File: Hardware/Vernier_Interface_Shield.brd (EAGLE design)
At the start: 76.2 x 71.1 mm, 44 parts, among them U1 74HC4052SO, U2 LMV358SOICT

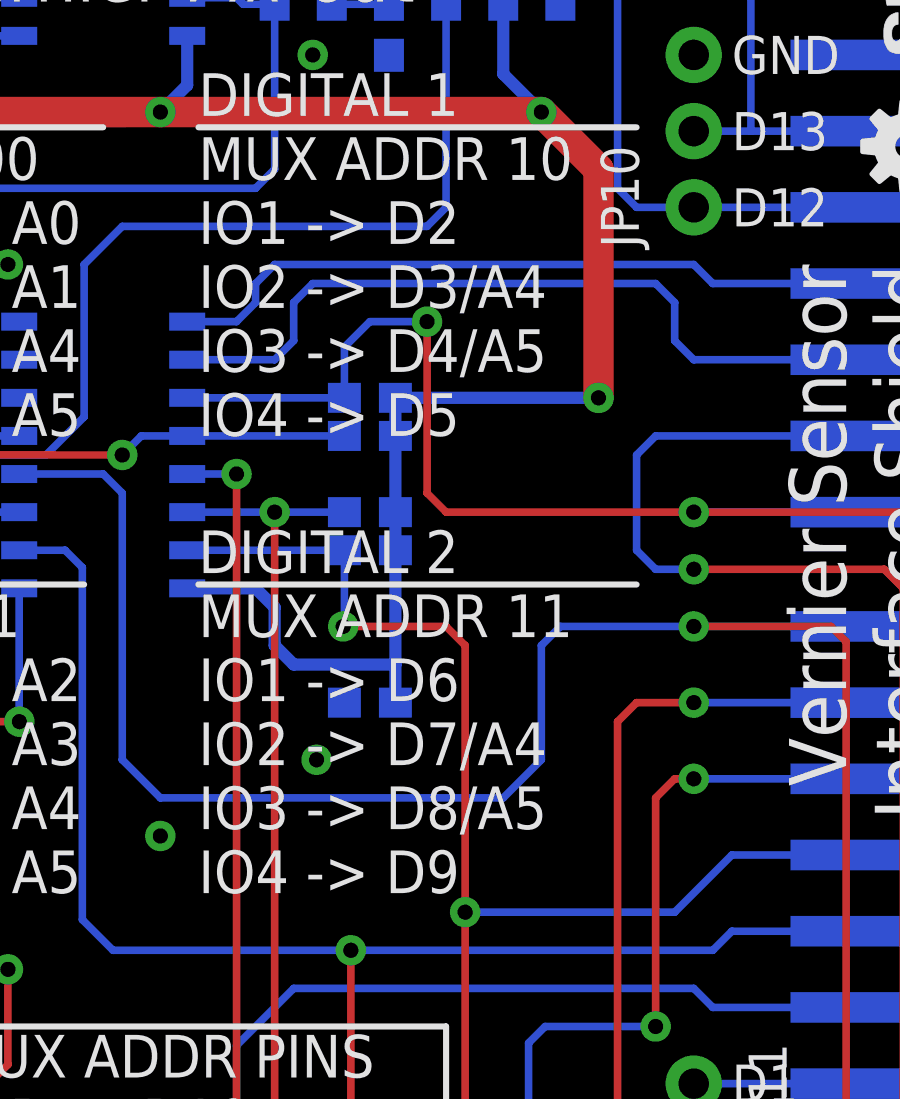
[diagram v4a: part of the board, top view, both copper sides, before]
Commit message: Changed silk to fix bug #4
Changed silk to start at IO0 instead of IO1. This is per Vernier's
request.
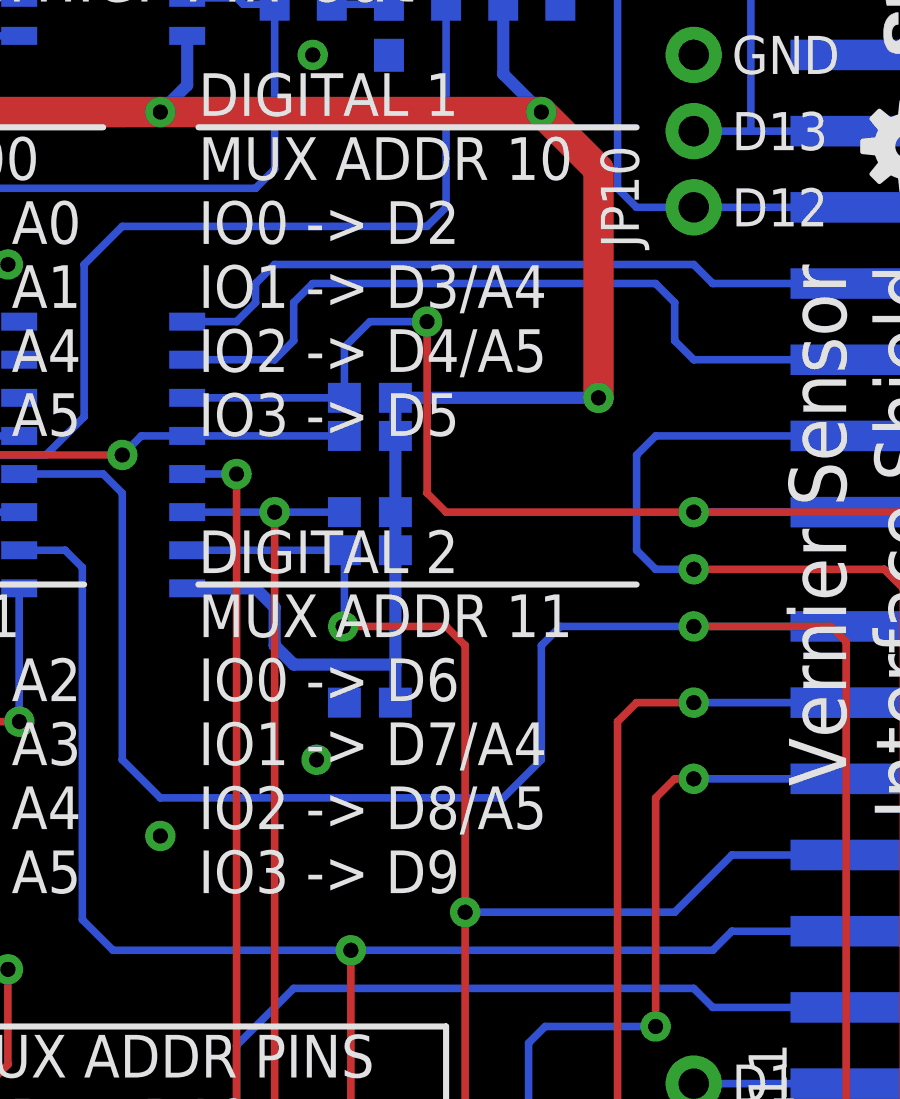
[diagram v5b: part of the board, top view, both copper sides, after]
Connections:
- removed net D1_IO4: JP2.6, JP7.6
- removed net D2_IO4: JP1.2, JP8.6
- new net D1_IO0: JP2.3, JP7.1
- new net D2_IO0: JP2.7, JP8.1
- net D1_IO1: now also JP2.4, JP7.2, U1.2; no longer JP2.3, JP7.1
- net D1_IO2: now also JP2.5, JP7.3, R17.2, U1.15; no longer JP2.4, JP7.2, U1.2
- net D1_IO3: now also JP2.6, JP7.6; no longer JP2.5, JP7.3, R17.2, U1.15
- net D2_IO1: now also JP2.8, JP8.2, U1.4; no longer JP2.7, JP8.1
- net D2_IO2: now also JP1.1, JP8.3, R18.2, U1.11; no longer JP2.8, JP8.2, U1.4
- net D2_IO3: now also JP1.2, JP8.6; no longer JP1.1, JP8.3, R18.2, U1.11
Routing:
- net D2_IO4: track 51.5 -> 0.00 mm, vias 1 -> 0
- net D2_IO0: track 0.00 -> 40.4 mm, vias 0 -> 2
- net D1_IO3: track 70.2 -> 30.6 mm, vias 3 -> 2
- net D1_IO0: track 0.00 -> 37.5 mm
- net D2_IO3: track 86.9 -> 51.5 mm, vias 2 -> 1
- net D2_IO1: track 40.4 -> 74.2 mm
- net D1_IO4: track 30.6 -> 0.00 mm, vias 2 -> 0
- net D1_IO1: track 37.5 -> 55.3 mm, vias 0 -> 1
- net D1_IO2: track 55.3 -> 70.2 mm, vias 1 -> 3
- net D2_IO2: track 74.2 -> 86.9 mm
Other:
- board text added: "DIGITAL 1 MUX ADDR 10 IO0 -> D2 IO1 -> D3/A4 IO2 -> D4/A5 IO3 -> D5"
- board text added: "DIGITAL 2 MUX ADDR 11 IO0 -> D6 IO1 -> D7/A4 IO2 -> D8/A5 IO3 -> D9"
- board text removed: "DIGITAL 1 MUX ADDR 10 IO1 -> D2 IO2 -> D3/A4 IO3 -> D4/A5 IO4 -> D5"
- board text removed: "DIGITAL 2 MUX ADDR 11 IO1 -> D6 IO2 -> D7/A4 IO3 -> D8/A5 IO4 -> D9"
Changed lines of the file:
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@@
 <text x="39.37" y="43.815" size="1.4224" layer="21" font="vector" ratio="15">DIGITAL 1
 MUX ADDR 10
-IO1 -&gt; D2
-IO2 -&gt; D3/A4
-IO3 -&gt; D4/A5
-IO4 -&gt; D5</text>
+IO0 -&gt; D2
+IO1 -&gt; D3/A4
+IO2 -&gt; D4/A5
+IO3 -&gt; D5</text>
 <text x="39.37" y="28.575" size="1.4224" layer="21" font="vector" ratio="15">DIGITAL 2
 MUX ADDR 11
-IO1 -&gt; D6
-IO2 -&gt; D7/A4
-IO3 -&gt; D8/A5
-IO4 -&gt; D9</text>
+IO0 -&gt; D6
+IO1 -&gt; D7/A4
+IO2 -&gt; D8/A5
+IO3 -&gt; D9</text>
 <text x="59.055" y="49.53" size="1.905" layer="21" font="vector" ratio="15" rot="R270">Vernier Sensor
 Interface Shield</text>
@@
 <wire x1="31.75" y1="17.78" x2="33.325" y2="16.205" width="0.254" layer="16"/>
 </signal>
-<signal name="D2_IO4">
+<signal name="D2_IO3">
 <contactref element="JP1" pad="2"/>
 <contactref element="JP8" pad="6"/>
@@
 <wire x1="65.405" y1="15.24" x2="62.865" y2="17.78" width="0.254" layer="1"/>
 </signal>
-<signal name="D2_IO3">
+<signal name="D2_IO2">
 <contactref element="U1" pad="11"/>
 <contactref element="R18" pad="2"/>
@@
 <wire x1="46.99" y1="41.91" x2="46.99" y2="47.625" width="0.254" layer="1"/>
 </signal>
-<signal name="D2_IO2">
+<signal name="D2_IO1">
 <contactref element="U1" pad="4"/>
 <contactref element="JP8" pad="2"/>
@@
 <wire x1="62.103" y1="37.465" x2="55.88" y2="37.465" width="0.254" layer="16"/>
 </signal>
-<signal name="D2_IO1">
+<signal name="D2_IO0">
 <contactref element="JP8" pad="1"/>
 <contactref element="JP2" pad="7"/>
@@
 <wire x1="53.34" y1="19.685" x2="54.61" y2="18.415" width="0.254" layer="1"/>
 </signal>
-<signal name="D1_IO4">
+<signal name="D1_IO3">
 <contactref element="JP7" pad="6"/>
 <via x="54.61" y="24.13" extent="1-16" drill="0.508"/>
@@
 <wire x1="55.245" y1="32.385" x2="54.61" y2="31.75" width="0.254" layer="1"/>
 </signal>
-<signal name="D1_IO3">
+<signal name="D1_IO2">
 <contactref element="U1" pad="15"/>
 <contactref element="R17" pad="2"/>
@@
 <wire x1="55.245" y1="27.94" x2="57.15" y2="29.845" width="0.254" layer="16"/>
 </signal>
-<signal name="D1_IO2">
+<signal name="D1_IO1">
 <contactref element="U1" pad="2"/>
 <contactref element="JP7" pad="2"/>
@@
 <wire x1="56.515" y1="26.67" x2="44.45" y2="26.67" width="0.254" layer="16"/>
 </signal>
-<signal name="D1_IO1">
+<signal name="D1_IO0">
 <contactref element="JP2" pad="3"/>
 <contactref element="JP7" pad="1"/>

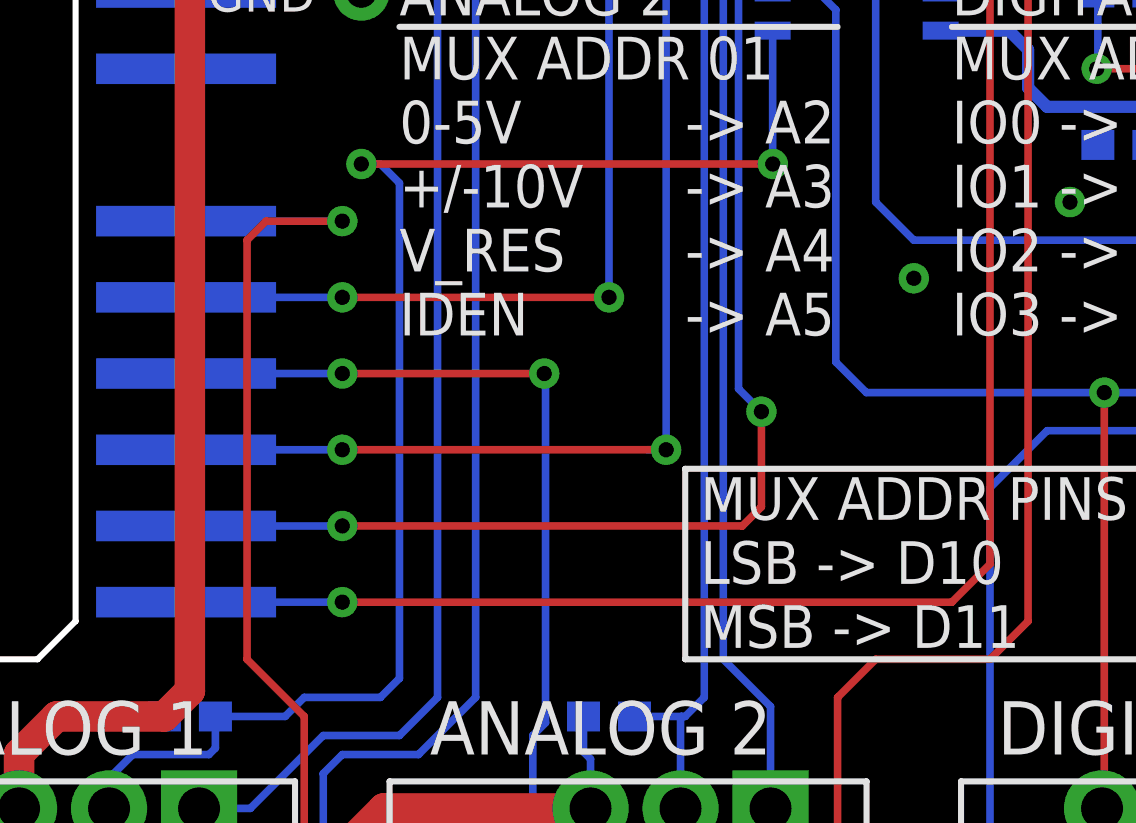
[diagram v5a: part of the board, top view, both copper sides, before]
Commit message: Updated A0-A5 vias to be exposed to allow for probe pins
Swapped out 6 vias on A0 to A5 with M06 for exposed copper vias to allow
for probe points
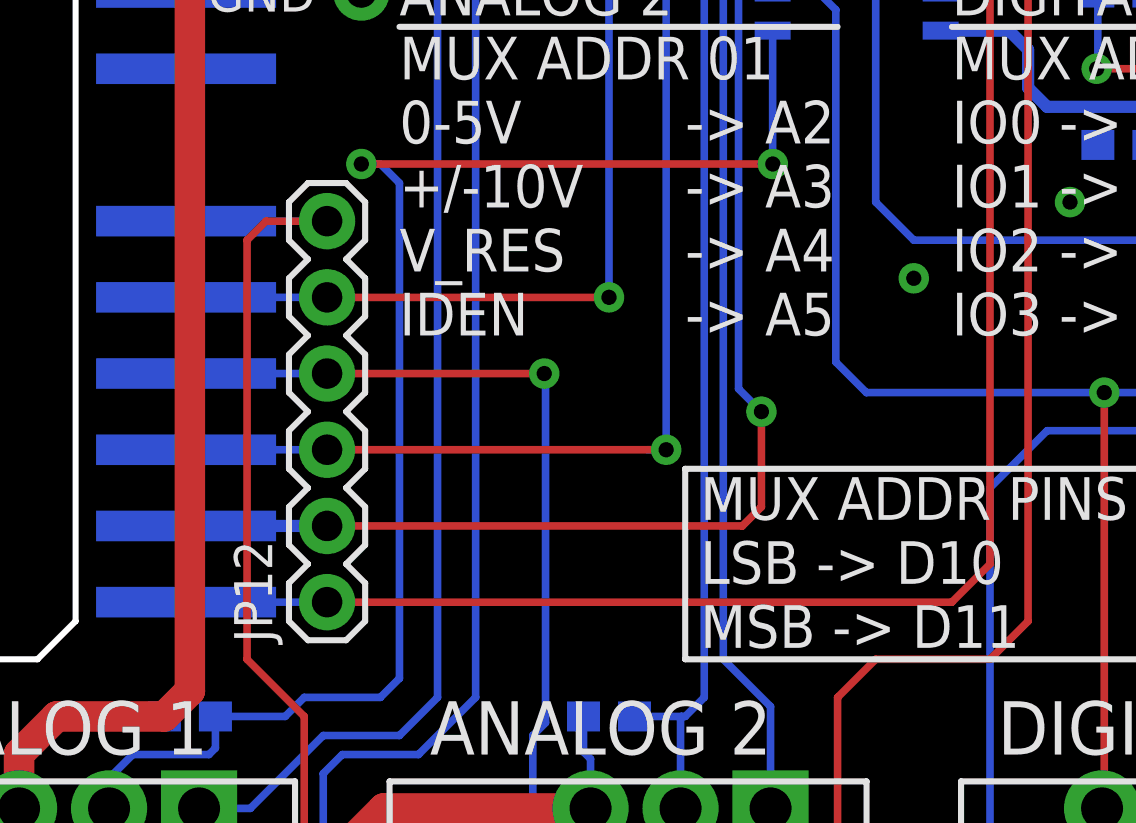
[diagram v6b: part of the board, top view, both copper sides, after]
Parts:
- added JP12: Male, SparkFun-Connectors:1X06
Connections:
- net A1: now also JP12.5
- net A3: now also JP12.3
- net A4: now also JP12.2
- net A5: now also JP12.1
- net AS1_AN2: now also JP12.6
- net AS2_AN2: now also JP12.4
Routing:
- net AS1_AN2: track 46.8 -> 45.8 mm, vias 1 -> 0
- net A5: vias 2 -> 1
- net AS2_AN2: vias 2 -> 1
- net A4: vias 2 -> 1
- net A3: vias 2 -> 1
- net A1: vias 2 -> 1
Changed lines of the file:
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@@
 </class>
 </classes>
-<designrules name="SparkFun *">
+<designrules name="SparkFun-2-layer">
 <description language="en">&lt;b&gt;EAGLE Design Rules&lt;/b&gt;
 &lt;p&gt;
@@
 <param name="mdDrill" value="8mil"/>
 <param name="mdSmdStop" value="0mil"/>
-<param name="msWidth" value="8mil"/>
-<param name="msDrill" value="20mil"/>
+<param name="msWidth" value="7mil"/>
+<param name="msDrill" value="15mil"/>
 <param name="msMicroVia" value="9.99mm"/>
 <param name="msBlindViaRatio" value="0.5"/>
@@
 <element name="S3" library="SparkFun-Electromechanical" package="TACTILE-PTH" value="Reset" x="16.51" y="67.31" rot="R180"/>
 <element name="S4" library="SparkFun-Electromechanical" package="TACTILE-PTH" value="D12" x="45.72" y="67.31" rot="R180"/>
+<element name="JP12" library="SparkFun-Connectors" package="1X06" value="Male" x="18.542" y="19.685" rot="R90"/>
 </elements>
 <signals>
@@
 <contactref element="JP4" pad="2"/>
 <contactref element="U1" pad="3"/>
-<wire x1="13.843" y1="22.225" x2="19.05" y2="22.225" width="0.254" layer="16"/>
-<via x="19.05" y="22.225" extent="1-16" drill="0.508"/>
 <wire x1="33.395" y1="41.275" x2="32.639" y2="41.275" width="0.254" layer="16"/>
 <wire x1="32.639" y1="41.275" x2="32.258" y2="40.894" width="0.254" layer="16"/>
@@
 <via x="33.02" y="26.035" extent="1-16" drill="0.508"/>
 <wire x1="32.258" y1="26.797" x2="33.02" y2="26.035" width="0.254" layer="16"/>
-<wire x1="19.05" y1="22.225" x2="32.385" y2="22.225" width="0.254" layer="1"/>
+<wire x1="18.542" y1="22.225" x2="32.385" y2="22.225" width="0.254" layer="1"/>
 <wire x1="32.385" y1="22.225" x2="33.02" y2="22.86" width="0.254" layer="1"/>
 <wire x1="33.02" y1="22.86" x2="33.02" y2="26.035" width="0.254" layer="1"/>
+<contactref element="JP12" pad="2"/>
+<wire x1="18.542" y1="22.225" x2="13.843" y2="22.225" width="0.4064" layer="16"/>
 </signal>
 <signal name="A5">
@@
 <wire x1="40.64" y1="42.545" x2="40.64" y2="20.955" width="0.254" layer="1"/>
 <wire x1="40.64" y1="20.955" x2="39.37" y2="19.685" width="0.254" layer="1"/>
-<wire x1="39.37" y1="19.685" x2="19.05" y2="19.685" width="0.254" layer="1"/>
-<via x="19.05" y="19.685" extent="1-16" drill="0.508"/>
-<wire x1="19.05" y1="19.685" x2="13.843" y2="19.685" width="0.254" layer="16"/>
+<wire x1="39.37" y1="19.685" x2="18.542" y2="19.685" width="0.254" layer="1"/>
+<wire x1="18.542" y1="19.685" x2="13.843" y2="19.685" width="0.254" layer="16"/>
+<contactref element="JP12" pad="1"/>
 </signal>
 <signal name="AREF">
@@
 <wire x1="15.875" y1="17.78" x2="15.875" y2="31.75" width="0.254" layer="1"/>
 <wire x1="15.875" y1="31.75" x2="16.51" y2="32.385" width="0.254" layer="1"/>
-<wire x1="16.51" y1="32.385" x2="19.05" y2="32.385" width="0.254" layer="1"/>
-<via x="19.05" y="32.385" extent="1-16" drill="0.508"/>
-<wire x1="19.05" y1="32.385" x2="13.843" y2="32.385" width="0.254" layer="16"/>
+<wire x1="16.51" y1="32.385" x2="18.542" y2="32.385" width="0.254" layer="1"/>
+<wire x1="18.542" y1="32.385" x2="13.843" y2="32.385" width="0.254" layer="16"/>
 <wire x1="15.875" y1="17.78" x2="17.78" y2="15.875" width="0.254" layer="1"/>
 <wire x1="17.78" y1="15.875" x2="17.78" y2="8.255" width="0.254" layer="1"/>
@@
 <wire x1="6.775" y1="9.81" x2="6.775" y2="7.83" width="0.254" layer="1"/>
 <wire x1="6.775" y1="7.83" x2="7.62" y2="6.985" width="0.254" layer="1"/>
+<contactref element="JP12" pad="6"/>
 </signal>
 <signal name="AS2_AN2">
 <contactref element="JP6" pad="6"/>
 <contactref element="JP4" pad="4"/>
-<wire x1="13.843" y1="27.305" x2="19.05" y2="27.305" width="0.254" layer="16"/>
-<via x="19.05" y="27.305" extent="1-16" drill="0.508"/>
-<wire x1="19.05" y1="27.305" x2="25.781" y2="27.305" width="0.254" layer="1"/>
+<wire x1="13.843" y1="27.305" x2="18.542" y2="27.305" width="0.254" layer="16"/>
+<wire x1="18.542" y1="27.305" x2="25.781" y2="27.305" width="0.254" layer="1"/>
 <via x="25.781" y="27.305" extent="1-16" drill="0.508"/>
 <wire x1="25.825" y1="27.261" x2="25.781" y2="27.305" width="0.254" layer="16"/>
@@
 <wire x1="25.825" y1="9.81" x2="25.825" y2="11.005" width="0.254" layer="16"/>
 <wire x1="25.825" y1="11.005" x2="25.4" y2="11.43" width="0.254" layer="16"/>
+<contactref element="JP12" pad="4"/>
 </signal>
 <signal name="AS2_AUTOID">
@@
 <contactref element="JP4" pad="5"/>
 <wire x1="27.94" y1="52.07" x2="27.94" y2="29.845" width="0.254" layer="16"/>
-<wire x1="13.843" y1="29.845" x2="19.05" y2="29.845" width="0.254" layer="16"/>
-<via x="19.05" y="29.845" extent="1-16" drill="0.508"/>
-<wire x1="19.05" y1="29.845" x2="27.94" y2="29.845" width="0.254" layer="1"/>
+<wire x1="13.843" y1="29.845" x2="18.542" y2="29.845" width="0.254" layer="16"/>
+<wire x1="18.542" y1="29.845" x2="27.94" y2="29.845" width="0.254" layer="1"/>
 <via x="27.94" y="29.845" extent="1-16" drill="0.508"/>
 <wire x1="27.94" y1="52.07" x2="30.48" y2="54.61" width="0.254" layer="16"/>
@@
 <wire x1="30.48" y1="56.935" x2="31.535" y2="56.935" width="0.254" layer="16"/>
 <wire x1="31.535" y1="56.935" x2="31.75" y2="57.15" width="0.254" layer="16"/>
+<contactref element="JP12" pad="5"/>
 </signal>
 <signal name="A3">
@@
 <contactref element="JP4" pad="3"/>
 <wire x1="38.995" y1="58.42" x2="40.64" y2="58.42" width="0.254" layer="16"/>
-<wire x1="13.843" y1="24.765" x2="19.05" y2="24.765" width="0.254" layer="16"/>
-<via x="19.05" y="24.765" extent="1-16" drill="0.508"/>
-<wire x1="19.05" y1="24.765" x2="29.845" y2="24.765" width="0.254" layer="1"/>
+<wire x1="13.843" y1="24.765" x2="18.542" y2="24.765" width="0.254" layer="16"/>
+<wire x1="18.542" y1="24.765" x2="29.845" y2="24.765" width="0.254" layer="1"/>
 <via x="29.845" y="24.765" extent="1-16" drill="0.508"/>
 <wire x1="29.845" y1="24.765" x2="29.21" y2="24.765" width="0.254" layer="16"/>
@@
 <wire x1="41.91" y1="58.205" x2="41.91" y2="52.705" width="0.254" layer="16"/>
 <wire x1="41.91" y1="52.705" x2="41.275" y2="52.07" width="0.254" layer="16"/>
+<contactref element="JP12" pad="3"/>
 </signal>
 <signal name="AS1_VRES">
